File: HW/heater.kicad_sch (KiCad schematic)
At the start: 3 parts

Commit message: Fixed board, big work in schematic, to finish
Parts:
- Q1: renamed from Q?; value (none) -> BUK9M156-100EX
- gave numbers to parts that had none: 2
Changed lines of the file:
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@@
   (symbol (lib_id "Device:Heater") (at 171.831 82.931 0) (unit 1)
     (in_bom yes) (on_board yes) (fields_autoplaced)
-    (property "Reference" "R?" (id 0) (at 173.609 82.0963 0)
+    (property "Reference" "R5" (id 0) (at 173.609 82.0963 0)
       (effects (font (size 1.27 1.27)) (justify left))
     )
@@
   (symbol (lib_id "Transistor_FET:BUK9M156-100EX") (at 169.291 94.361 0) (unit 1)
     (in_bom yes) (on_board yes) (fields_autoplaced)
-    (property "Reference" "Q?" (id 0) (at 174.498 93.5263 0)
+    (property "Reference" "Q1" (id 0) (at 174.498 93.5263 0)
       (effects (font (size 1.27 1.27)) (justify left))
     )
-    (property "Value" "" (id 1) (at 174.498 96.0632 0)
+    (property "Value" "BUK9M156-100EX" (id 1) (at 174.498 96.0632 0)
       (effects (font (size 1.27 1.27)) (justify left))
     )
@@
   (symbol (lib_id "power:+12V") (at 171.831 76.581 0) (unit 1)
     (in_bom yes) (on_board yes) (fields_autoplaced)
-    (property "Reference" "#PWR?" (id 0) (at 171.831 80.391 0)
+    (property "Reference" "#PWR0109" (id 0) (at 171.831 80.391 0)
       (effects (font (size 1.27 1.27)) hide)
     )
@@
   (symbol (lib_id "power:GND") (at 171.831 110.871 0) (unit 1)
     (in_bom yes) (on_board yes) (fields_autoplaced)
-    (property "Reference" "#PWR?" (id 0) (at 171.831 117.221 0)
+    (property "Reference" "#PWR0108" (id 0) (at 171.831 117.221 0)
       (effects (font (size 1.27 1.27)) hide)
     )
@@
   (symbol (lib_id "Device:R") (at 161.036 98.171 0) (unit 1)
     (in_bom yes) (on_board yes)
-    (property "Reference" "R?" (id 0) (at 161.036 98.171 90))
+    (property "Reference" "R4" (id 0) (at 161.036 98.171 90))
     (property "Value" "10k" (id 1) (at 158.8571 98.171 90))
     (property "Footprint" "" (id 2) (at 159.258 98.171 90)

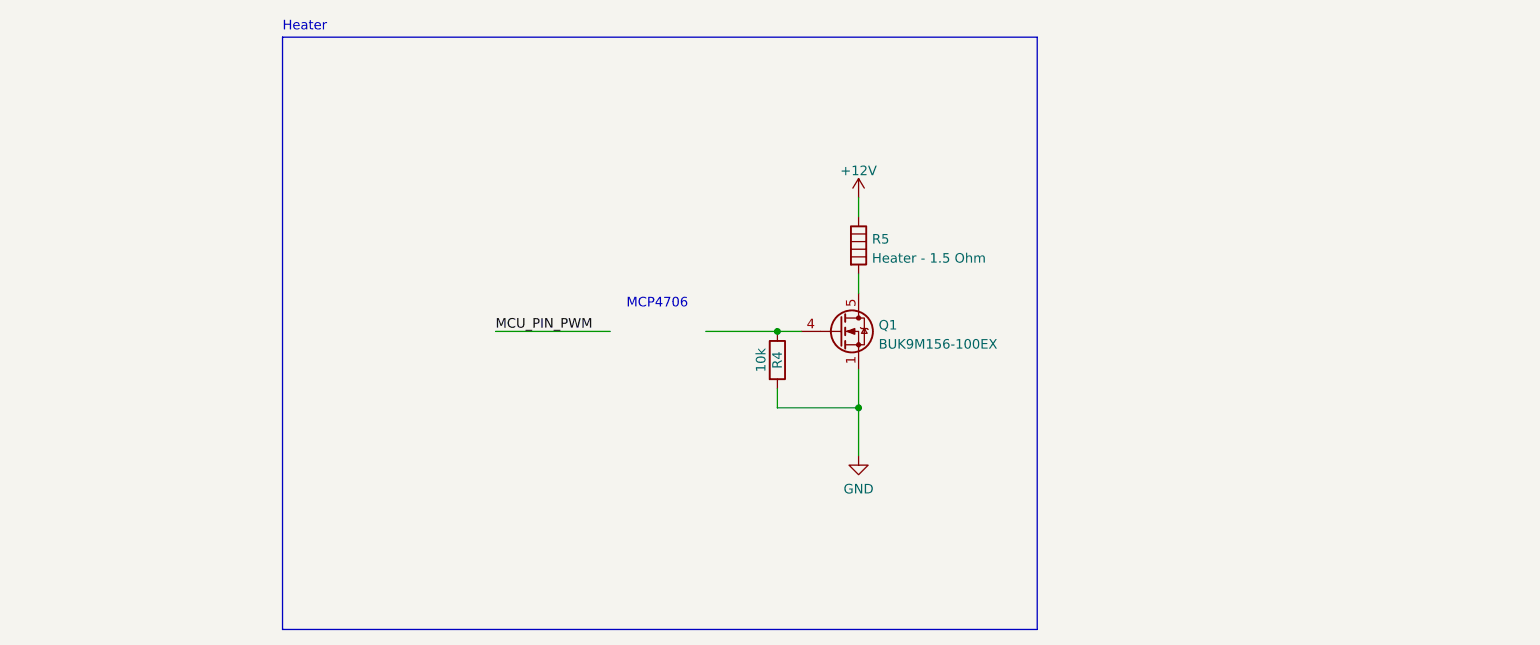
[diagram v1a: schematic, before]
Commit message: Finished sch, to be checked. Initial components layout
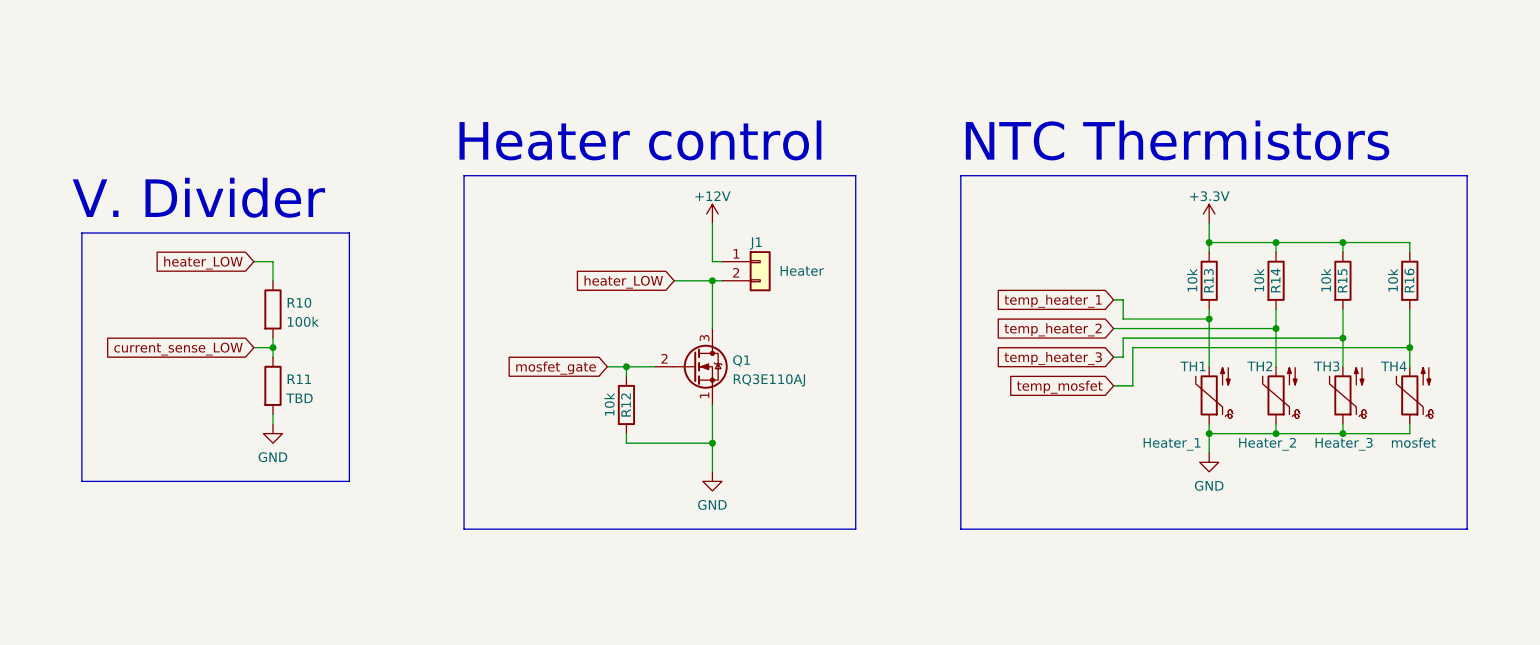
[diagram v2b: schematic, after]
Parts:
- removed Q1: BUK9M156-100EX, Package_TO_SOT_SMD:LFPAK33, symbol Transistor_FET:BUK9M156-100EX
- removed R4: 10k, symbol Device:R
- removed R5: Heater - 1.5 Ohm, symbol Device:Heater
- added J1: Heater, TerminalBlock:TerminalBlock_bornier-2_P5.08mm, symbol Connector_Generic:Conn_01x02
- added Q1: RQ3E110AJ, SOTFL65P330X80-8N:SOTFL65P330X80-8N, symbol RQ3E100GNTB:RQ3E110AJ
- added R10: 100k, symbol Device:R
- added R11: TBD, symbol Device:R
- added R12, R13, R14, R15, R16: 10k, Resistor_SMD:R_0603_1608Metric, symbol Device:R
- added TH1: Heater_1, Connector_PinHeader_2.54mm:PinHeader_1x02_P2.54mm_Vertical, symbol Device:Thermistor_NTC
- added TH2: Heater_2, Connector_PinHeader_2.54mm:PinHeader_1x02_P2.54mm_Vertical, symbol Device:Thermistor_NTC
- added TH3: Heater_3, Connector_PinHeader_2.54mm:PinHeader_1x02_P2.54mm_Vertical, symbol Device:Thermistor_NTC
- added TH4: mosfet, Connector_PinHeader_2.54mm:PinHeader_1x02_P2.54mm_Vertical, symbol Device:Thermistor_NTC
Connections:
- net +12V: now also J1.1 (Pin_1)
- net GND: now also Q1.1 (S), R11.2, R12.2, TH1.1, TH2.1, TH3.1, TH4.1
- new net +3V3: R13.1, R14.1, R15.1, R16.1
- new net current_sense_LOW: R10.2, R11.1
- new net heater_LOW: J1.2 (Pin_2), Q1.3 (D), R10.1
- new net mosfet_gate: Q1.2 (G), R12.1
- new net temp_heater_1: R13.2, TH1.2
- new net temp_heater_2: R14.2, TH2.2
- new net temp_heater_3: R15.2, TH3.2
- new net temp_mosfet: R16.2, TH4.2
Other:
- note added: "Heater control"
- note added: "NTC Thermistors"
- note added: "V. Divider"
- note removed: "Heater"
- note removed: "MCP4706"

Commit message: Sch finalized, added EMC stuff, user buttons and oled
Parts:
- R10, R11: footprint (none) -> Resistor_SMD:R_0603_1608Metric
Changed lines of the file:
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@@
       (effects (font (size 1.27 1.27)) (justify left))
     )
-    (property "Footprint" "" (id 2) (at 92.202 101.6 90)
+    (property "Footprint" "Resistor_SMD:R_0603_1608Metric" (id 2) (at 92.202 101.6 90)
       (effects (font (size 1.27 1.27)) hide)
     )
@@
       (effects (font (size 1.27 1.27)) (justify left))
     )
-    (property "Footprint" "" (id 2) (at 92.202 91.44 90)
+    (property "Footprint" "Resistor_SMD:R_0603_1608Metric" (id 2) (at 92.202 91.44 90)
       (effects (font (size 1.27 1.27)) hide)
     )

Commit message: Work on layout, sch fixes, added several 3d models
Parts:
- J1: footprint TerminalBlock:TerminalBlock_bornier-2_P5.08mm -> WR_TBL_Series_101:WR_TBL_Series_101
- R11: value TBD -> 37k
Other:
- note added: "- low side resistor should be 37931"
- moved on the sheet: R10, R11
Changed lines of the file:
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@@
   (junction (at 218.44 82.55) (diameter 0) (color 0 0 0 0)
   )
-  (junction (at 93.98 96.52) (diameter 0) (color 0 0 0 0)
+  (junction (at 97.79 97.79) (diameter 0) (color 0 0 0 0)
   )
   (junction (at 236.22 107.95) (diameter 0) (color 0 0 0 0)
@@
     (stroke (width 0) (type default) (color 0 0 0 0))
   )
-  (wire (pts (xy 91.44 85.09) (xy 93.98 85.09))
-    (stroke (width 0) (type default) (color 0 0 0 0))
-  )
   (wire (pts (xy 227.33 82.55) (xy 236.22 82.55))
     (stroke (width 0) (type default) (color 0 0 0 0))
   )
-  (wire (pts (xy 91.44 96.52) (xy 93.98 96.52))
+  (wire (pts (xy 95.25 97.79) (xy 97.79 97.79))
     (stroke (width 0) (type default) (color 0 0 0 0))
   )
@@
     (stroke (width 0) (type default) (color 0 0 0 0))
   )
-  (wire (pts (xy 93.98 85.09) (xy 93.98 87.63))
-    (stroke (width 0) (type default) (color 0 0 0 0))
-  )
-  (wire (pts (xy 93.98 96.52) (xy 93.98 97.79))
+  (wire (pts (xy 97.79 86.36) (xy 97.79 88.9))
+    (stroke (width 0) (type default) (color 0 0 0 0))
+  )
+  (wire (pts (xy 97.79 97.79) (xy 97.79 99.06))
     (stroke (width 0) (type default) (color 0 0 0 0))
   )
@@
     (stroke (width 0) (type default) (color 0 0 0 0))
   )
-  (polyline (pts (xy 68.58 81.28) (xy 68.58 114.3))
+  (polyline (pts (xy 68.58 81.28) (xy 68.58 119.38))
     (stroke (width 0) (type default) (color 0 0 0 0))
   )
@@
     (stroke (width 0) (type default) (color 0 0 0 0))
   )
-  (polyline (pts (xy 68.58 114.3) (xy 104.14 114.3))
-    (stroke (width 0) (type default) (color 0 0 0 0))
-  )
-  (polyline (pts (xy 68.58 81.28) (xy 104.14 81.28))
+  (polyline (pts (xy 68.58 119.38) (xy 109.22 119.38))
+    (stroke (width 0) (type default) (color 0 0 0 0))
+  )
+  (polyline (pts (xy 68.58 81.28) (xy 109.22 81.28))
     (stroke (width 0) (type default) (color 0 0 0 0))
   )
@@
     (stroke (width 0) (type default) (color 0 0 0 0))
   )
-  (polyline (pts (xy 104.14 114.3) (xy 104.14 81.28))
+  (polyline (pts (xy 109.22 119.38) (xy 109.22 81.28))
     (stroke (width 0) (type default) (color 0 0 0 0))
   )
@@
     (stroke (width 0) (type default) (color 0 0 0 0))
   )
-  (wire (pts (xy 93.98 105.41) (xy 93.98 106.68))
+  (wire (pts (xy 97.79 106.68) (xy 97.79 107.95))
     (stroke (width 0) (type default) (color 0 0 0 0))
   )
@@
     (stroke (width 0) (type default) (color 0 0 0 0))
   )
-  (wire (pts (xy 93.98 95.25) (xy 93.98 96.52))
+  (wire (pts (xy 97.79 96.52) (xy 97.79 97.79))
     (stroke (width 0) (type default) (color 0 0 0 0))
   )
@@
     (effects (font (size 5 5)) (justify left bottom))
   )
+  (text "- low side resistor should be 37931" (at 69.85 118.11 0)
+    (effects (font (size 1.27 1.27)) (justify left bottom))
+  )
   (text "Heater control" (at 118.11 72.39 0)
     (effects (font (size 5 5)) (justify left bottom))
   )
-  (global_label "heater_LOW" (shape input) (at 147.32 87.63 180) (fields_autoplaced)
-    (effects (font (size 1.27 1.27)) (justify right))
-    (property "Intersheet References" "${INTERSHEET_REFS}" (id 0) (at 134.1421 87.5506 0)
-      (effects (font (size 1.27 1.27)) (justify right) hide)
-    )
+  (label "heater_LOW" (at 147.32 87.63 180)
+    (effects (font (size 1.27 1.27)) (justify right bottom))
+  )
+  (label "heater_LOW" (at 97.79 86.36 180)
+    (effects (font (size 1.27 1.27)) (justify right bottom))
   )
   (global_label "temp_heater_3" (shape input) (at 205.74 97.79 180) (fields_autoplaced)
@@
     )
   )
-  (global_label "heater_LOW" (shape input) (at 91.44 85.09 180) (fields_autoplaced)
-    (effects (font (size 1.27 1.27)) (justify right))
-    (property "Intersheet References" "${INTERSHEET_REFS}" (id 0) (at 78.2621 85.0106 0)
-      (effects (font (size 1.27 1.27)) (justify right) hide)
-    )
-  )
-  (global_label "current_sense_LOW" (shape input) (at 91.44 96.52 180) (fields_autoplaced)
-    (effects (font (size 1.27 1.27)) (justify right))
-    (property "Intersheet References" "${INTERSHEET_REFS}" (id 0) (at 71.1259 96.5994 0)
+  (global_label "current_sense_LOW" (shape input) (at 95.25 97.79 180) (fields_autoplaced)
+    (effects (font (size 1.27 1.27)) (justify right))
+    (property "Intersheet References" "${INTERSHEET_REFS}" (id 0) (at 74.9359 97.8694 0)
       (effects (font (size 1.27 1.27)) (justify right) hide)
     )
@@
     (pin "2")
   )
-  (symbol (lib_id "power:GND") (at 93.98 106.68 0) (unit 1)
-    (in_bom yes) (on_board yes) (fields_autoplaced)
-    (property "Reference" "#PWR0115" (id 0) (at 93.98 113.03 0)
-      (effects (font (size 1.27 1.27)) hide)
-    )
-    (property "Value" "GND" (id 1) (at 93.98 111.1234 0))
-    (property "Footprint" "" (id 2) (at 93.98 106.68 0)
-      (effects (font (size 1.27 1.27)) hide)
-    )
-    (property "Datasheet" "" (id 3) (at 93.98 106.68 0)
+  (symbol (lib_id "power:GND") (at 97.79 107.95 0) (unit 1)
+    (in_bom yes) (on_board yes) (fields_autoplaced)
+    (property "Reference" "#PWR0115" (id 0) (at 97.79 114.3 0)
+      (effects (font (size 1.27 1.27)) hide)
+    )
+    (property "Value" "GND" (id 1) (at 97.79 112.3934 0))
+    (property "Footprint" "" (id 2) (at 97.79 107.95 0)
+      (effects (font (size 1.27 1.27)) hide)
+    )
+    (property "Datasheet" "" (id 3) (at 97.79 107.95 0)
       (effects (font (size 1.27 1.27)) hide)
     )
@@
       (effects (font (size 1.27 1.27)) (justify left))
     )
-    (property "Footprint" "TerminalBlock:TerminalBlock_bornier-2_P5.08mm" (id 2) (at 158.75 85.09 0)
+    (property "Footprint" "WR_TBL_Series_101:WR_TBL_Series_101" (id 2) (at 158.75 85.09 0)
       (effects (font (size 1.27 1.27)) hide)
     )
@@
     (pin "1")
   )
-  (symbol (lib_id "Device:R") (at 93.98 101.6 0) (unit 1)
-    (in_bom yes) (on_board yes) (fields_autoplaced)
-    (property "Reference" "R11" (id 0) (at 95.758 100.7653 0)
-      (effects (font (size 1.27 1.27)) (justify left))
-    )
-    (property "Value" "TBD" (id 1) (at 95.758 103.3022 0)
-      (effects (font (size 1.27 1.27)) (justify left))
-    )
-    (property "Footprint" "Resistor_SMD:R_0603_1608Metric" (id 2) (at 92.202 101.6 90)
-      (effects (font (size 1.27 1.27)) hide)
-    )
-    (property "Datasheet" "~" (id 3) (at 93.98 101.6 0)
-      (effects (font (size 1.27 1.27)) hide)
-    )
-    (pin "1")
-    (pin "2")
-  )
-  (symbol (lib_id "Device:R") (at 93.98 91.44 0) (unit 1)
-    (in_bom yes) (on_board yes) (fields_autoplaced)
-    (property "Reference" "R10" (id 0) (at 95.758 90.6053 0)
-      (effects (font (size 1.27 1.27)) (justify left))
-    )
-    (property "Value" "100k" (id 1) (at 95.758 93.1422 0)
-      (effects (font (size 1.27 1.27)) (justify left))
-    )
-    (property "Footprint" "Resistor_SMD:R_0603_1608Metric" (id 2) (at 92.202 91.44 90)
-      (effects (font (size 1.27 1.27)) hide)
-    )
-    (property "Datasheet" "~" (id 3) (at 93.98 91.44 0)
-      (effects (font (size 1.27 1.27)) hide)
-    )
+  (symbol (lib_id "Device:R") (at 97.79 102.87 0) (unit 1)
+    (in_bom yes) (on_board yes) (fields_autoplaced)
+    (property "Reference" "R11" (id 0) (at 99.568 102.0353 0)
+      (effects (font (size 1.27 1.27)) (justify left))
+    )
+    (property "Value" "37k" (id 1) (at 99.568 104.5722 0)
+      (effects (font (size 1.27 1.27)) (justify left))
+    )
+    (property "Footprint" "Resistor_SMD:R_0603_1608Metric" (id 2) (at 96.012 102.87 90)
+      (effects (font (size 1.27 1.27)) hide)
+    )
+    (property "Datasheet" "~" (id 3) (at 97.79 102.87 0)
+      (effects (font (size 1.27 1.27)) hide)
+    )
+    (pin "1")
+    (pin "2")
+  )
+  (symbol (lib_id "Device:R") (at 97.79 92.71 0) (unit 1)
+    (in_bom yes) (on_board yes) (fields_autoplaced)
+    (property "Reference" "R10" (id 0) (at 99.568 91.8753 0)
+      (effects (font (size 1.27 1.27)) (justify left))
+    )
+    (property "Value" "100k" (id 1) (at 99.568 94.4122 0)
+      (effects (font (size 1.27 1.27)) (justify left))
+    )
+    (property "Footprint" "Resistor_SMD:R_0603_1608Metric" (id 2) (at 96.012 92.71 90)
+      (effects (font (size 1.27 1.27)) hide)
+    )
+    (property "Datasheet" "~" (id 3) (at 97.79 92.71 0)
+      (effects (font (size 1.27 1.27)) hide)
+    )

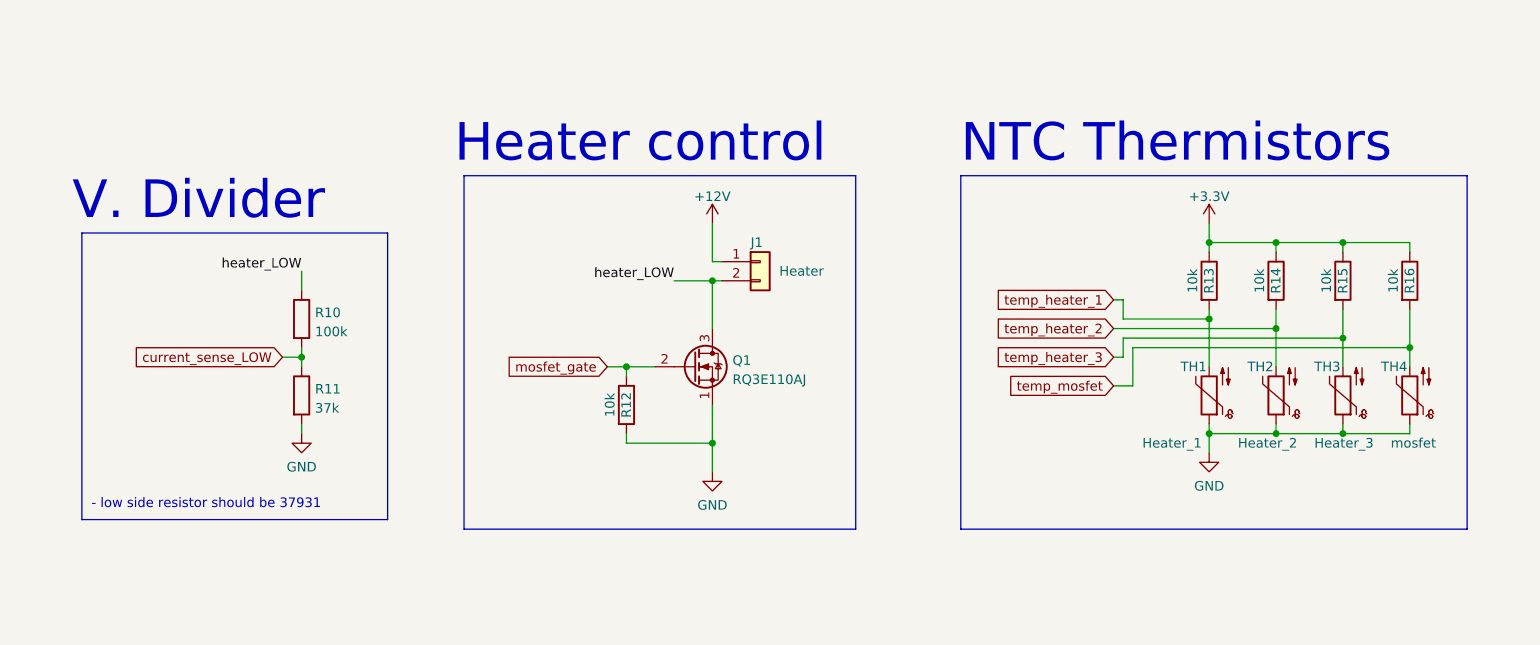
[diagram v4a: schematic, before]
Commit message: starterd routing, removed OTG usb port
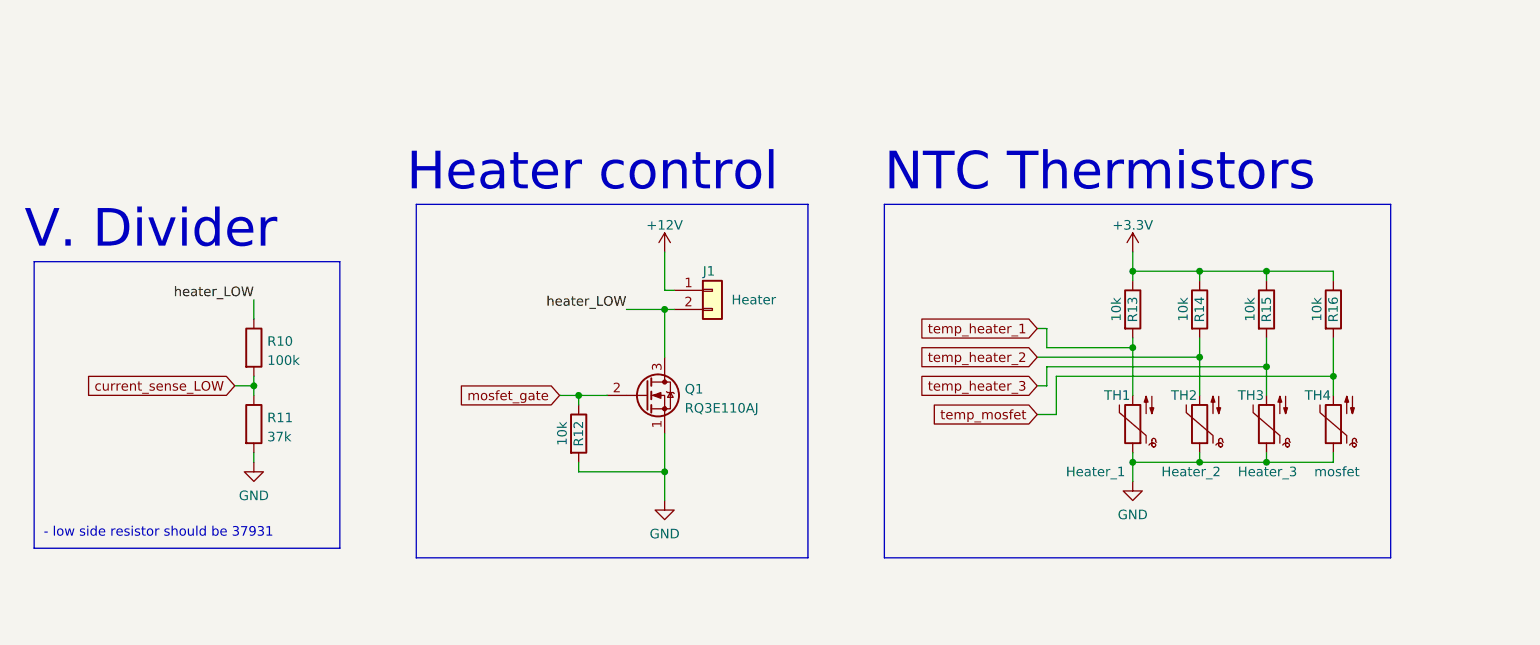
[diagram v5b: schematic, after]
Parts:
- TH1, TH2, TH3, TH4: footprint Connector_PinHeader_2.54mm:PinHeader_1x02_P2.54mm_Vertical -> TestPoint:TestPoint_2Pads_Pitch2.54mm_Drill0.8mm
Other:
- moved on the sheet: J1, Q1, R10, R11, R12, R13, R14, R15, R16, TH1, TH2, TH3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
